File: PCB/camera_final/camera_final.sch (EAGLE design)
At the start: 4 parts

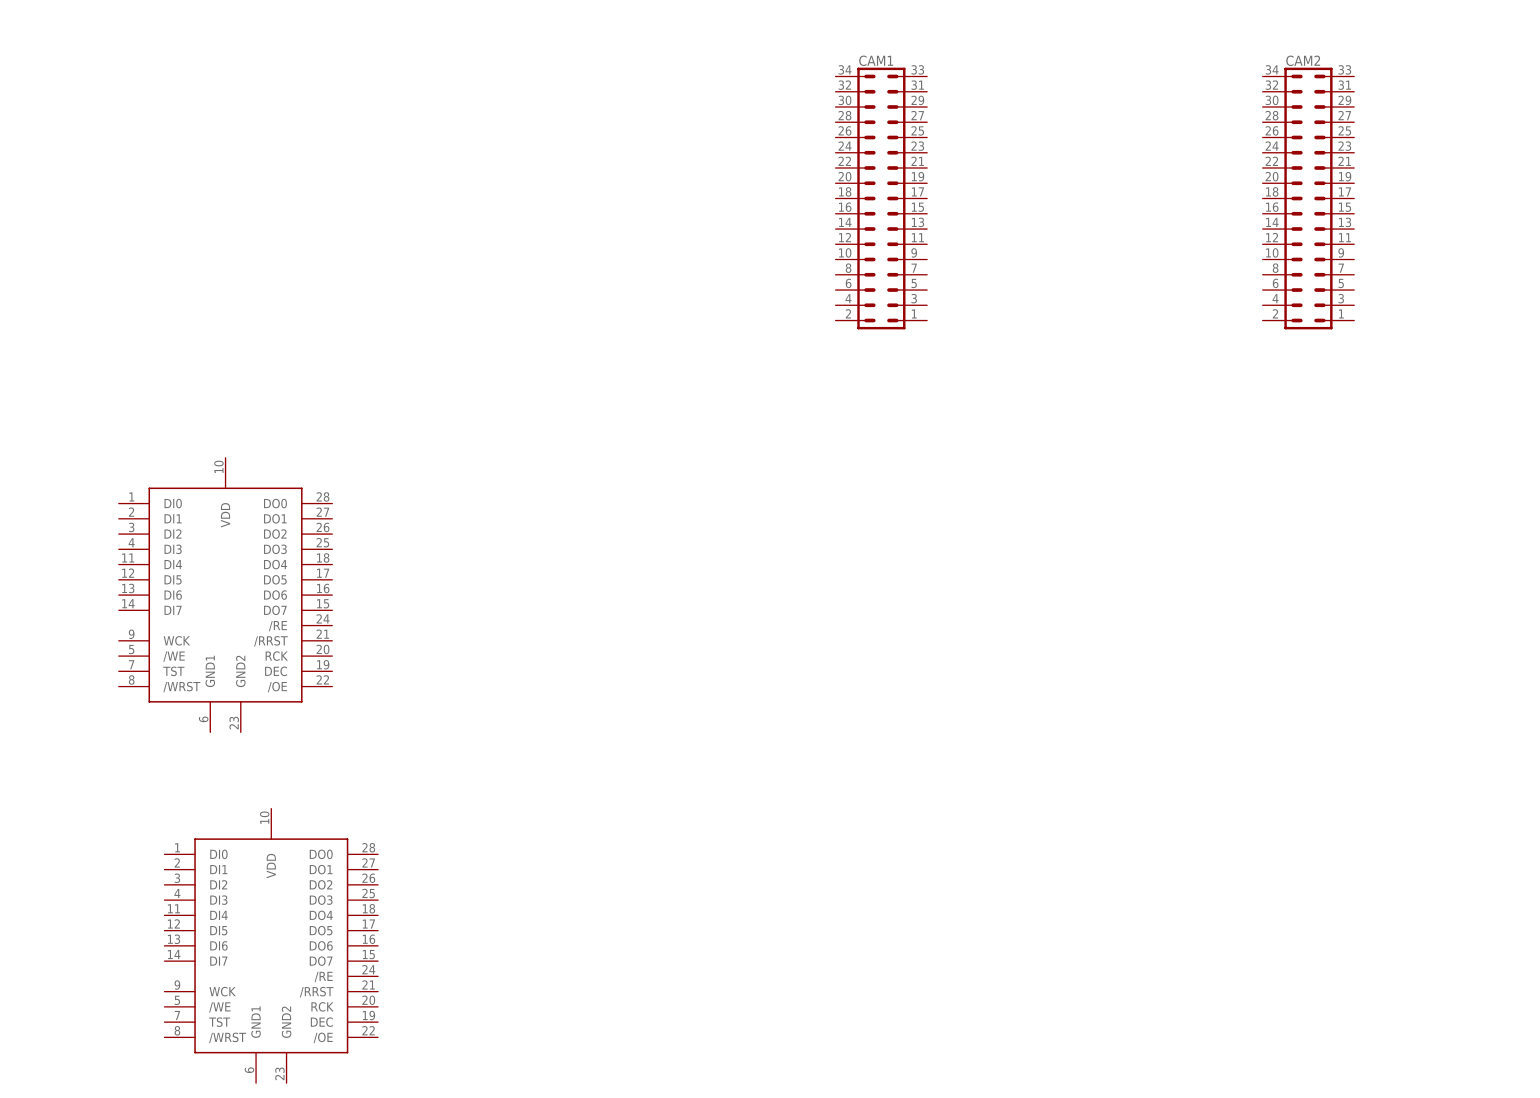
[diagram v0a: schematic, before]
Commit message: final stereo cam schematic, started layout
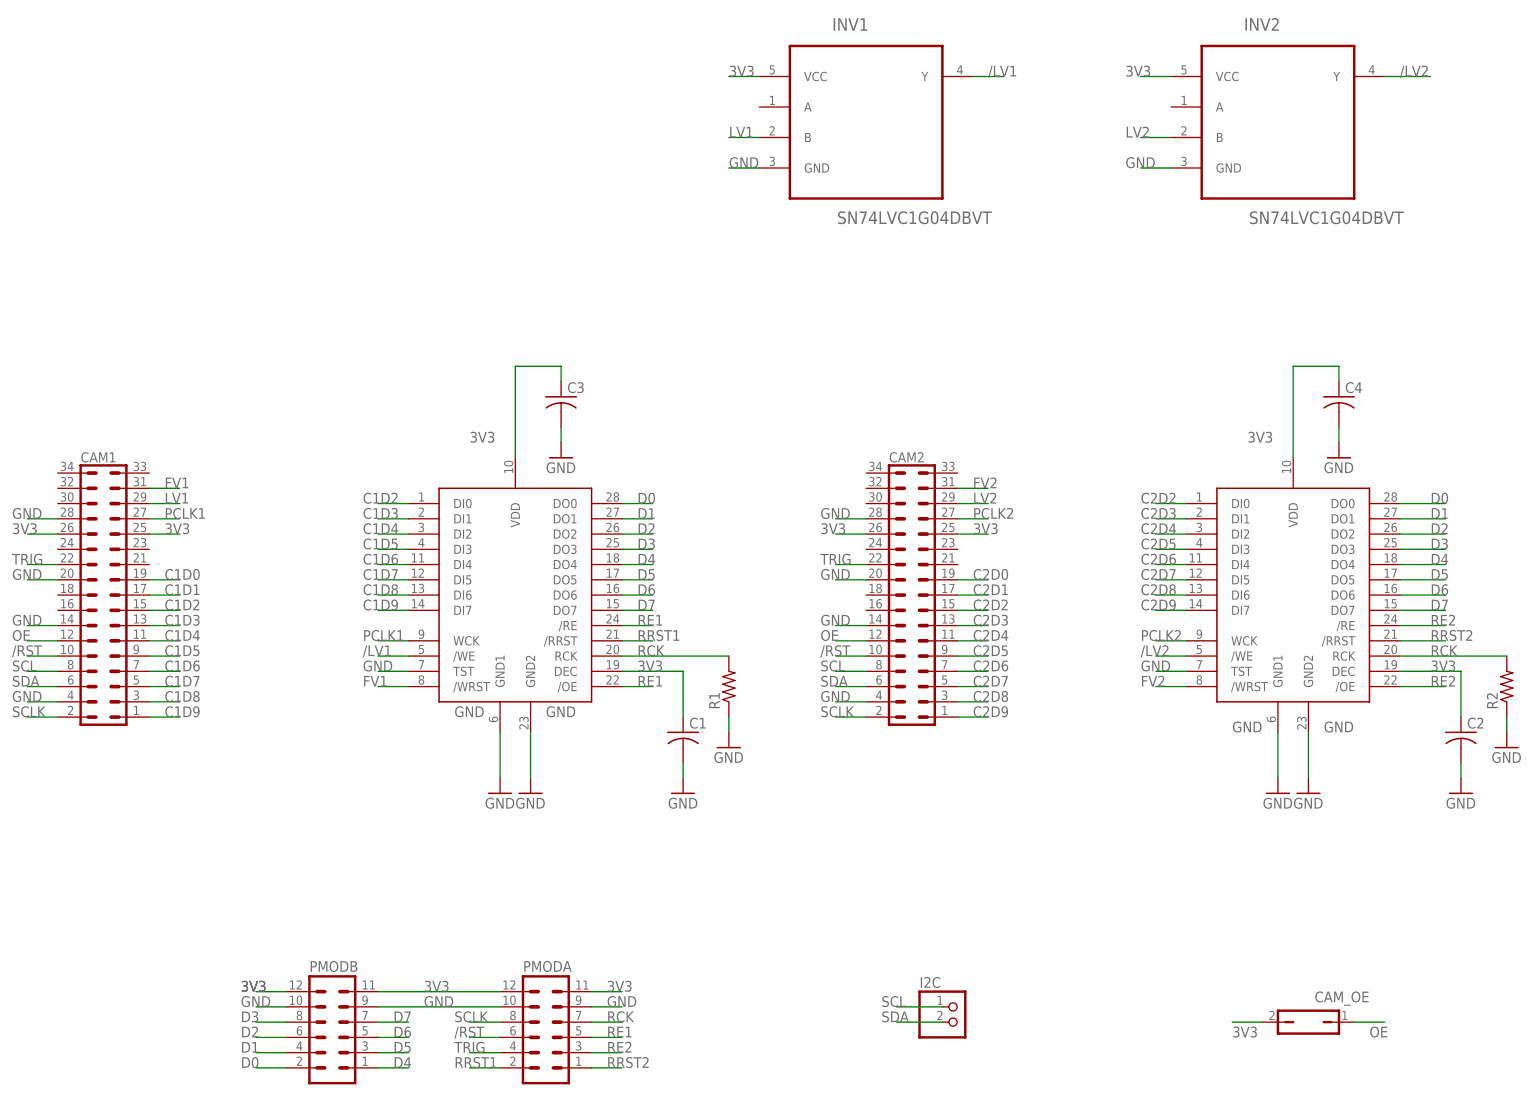
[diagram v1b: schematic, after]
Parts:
- added C1, C2, C3, C4: (no value), adafruit:C-USC0805K
- added CAM_OE: (no value), jumper:JP1Q
- added I2C: (no value), pinhead:PINHD-1X2
- added INV1, INV2: SN74LVC1G04DBVT, Texas Instruments_By_element14_Batch_1:SN74LVC1G08DBVT
- added PMODA, PMODB: (no value), con-lstb:MA06-2
- added R1, R2: (no value), rcl:R-US_R0805
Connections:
- new net /LV1: INV1.Y, U$2./WE
- new net /LV2: INV2.Y, U$1./WE
- new net /RST: CAM1.10, CAM2.10, PMODA.6
- new net 3V3: C1.1, C2.1, C3.1, C4.1, CAM1.25, CAM1.26, CAM2.25, CAM2.26, CAM_OE.2, INV1.VCC, INV2.VCC, PMODA.11, PMODA.12, PMODB.11, PMODB.12, U$1.DEC, U$1.VDD, U$2.DEC, U$2.VDD
- new net C1D0: CAM1.19
- new net C1D1: CAM1.17
- new net C1D2: CAM1.15, U$2.DI0
- new net C1D3: CAM1.13, U$2.DI1
- new net C1D4: CAM1.11, U$2.DI2
- new net C1D5: CAM1.9, U$2.DI3
- new net C1D6: CAM1.7, U$2.DI4
- new net C1D7: CAM1.5, U$2.DI5
- new net C1D8: CAM1.3, U$2.DI6
- new net C1D9: CAM1.1, U$2.DI7
- new net C2D0: CAM2.19
- new net C2D1: CAM2.17
- new net C2D2: CAM2.15, U$1.DI0
- new net C2D3: CAM2.13, U$1.DI1
- new net C2D4: CAM2.11, U$1.DI2
- new net C2D5: CAM2.9, U$1.DI3
- new net C2D6: CAM2.7, U$1.DI4
- new net C2D7: CAM2.5, U$1.DI5
- new net C2D8: CAM2.3, U$1.DI6
- new net C2D9: CAM2.1, U$1.DI7
- new net D0: PMODB.2, U$1.DO0, U$2.DO0
- new net D1: PMODB.4, U$1.DO1, U$2.DO1
- new net D2: PMODB.6, U$1.DO2, U$2.DO2
- new net D3: PMODB.8, U$1.DO3, U$2.DO3
- new net D4: PMODB.1, U$1.DO4, U$2.DO4
- new net D5: PMODB.3, U$1.DO5, U$2.DO5
- new net D6: PMODB.5, U$1.DO6, U$2.DO6
- new net D7: PMODB.7, U$1.DO7, U$2.DO7
- new net FV1: CAM1.31, U$2./WRST
- new net FV2: CAM2.31, U$1./WRST
- new net GND: C1.2, C2.2, C3.2, C4.2, CAM1.14, CAM1.20, CAM1.28, CAM1.4, CAM2.14, CAM2.20, CAM2.28, CAM2.4, INV1.GND, INV2.GND, PMODA.10, PMODA.9, PMODB.10, PMODB.9, R1.1, R2.1, U$1.GND1, U$1.GND2, U$1.TST, U$2.GND1, U$2.GND2, U$2.TST
- new net LV1: CAM1.29, INV1.B
- new net LV2: CAM2.29, INV2.B
- new net OE: CAM1.12, CAM2.12, CAM_OE.1
- new net PCLK1: CAM1.27, U$2.WCK
- new net PCLK2: CAM2.27, U$1.WCK
- new net RCK: PMODA.7, R1.2, R2.2, U$1.RCK, U$2.RCK
- new net RE1: PMODA.5, U$2./OE, U$2./RE
- new net RE2: PMODA.3, U$1./OE, U$1./RE
- new net RRST1: PMODA.2, U$2./RRST
- new net RRST2: PMODA.1, U$1./RRST
- new net SCL: CAM1.8, CAM2.8, I2C.1
- new net SCLK: CAM1.2, CAM2.2, PMODA.8
- new net SDA: CAM1.6, CAM2.6, I2C.2
- new net TRIG: CAM1.22, CAM2.22, PMODA.4
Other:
- moved on the sheet: CAM1, CAM2

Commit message: semi-finalized layout
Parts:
- removed R2: (no value), rcl:R-US_R0805
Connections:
- net GND: no longer R2.1
- net RCK: no longer R2.2
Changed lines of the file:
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@@
 <part name="I2C" library="pinhead" deviceset="PINHD-1X2" device=""/>
 <part name="R1" library="rcl" deviceset="R-US_" device="R0805"/>
-<part name="R2" library="rcl" deviceset="R-US_" device="R0805"/>
 <part name="GND1" library="SparkFun-Aesthetics" deviceset="GND" device=""/>
 <part name="GND2" library="SparkFun-Aesthetics" deviceset="GND" device=""/>
-<part name="GND3" library="SparkFun-Aesthetics" deviceset="GND" device=""/>
 <part name="GND4" library="SparkFun-Aesthetics" deviceset="GND" device=""/>
 <part name="GND5" library="SparkFun-Aesthetics" deviceset="GND" device=""/>
@@
 <instance part="I2C" gate="G$1" x="170.18" y="40.64"/>
 <instance part="R1" gate="G$1" x="132.08" y="96.52" rot="R90"/>
-<instance part="R2" gate="G$1" x="261.62" y="96.52" rot="R90"/>
 <instance part="GND1" gate="1" x="223.52" y="78.74"/>
 <instance part="GND2" gate="1" x="228.6" y="78.74"/>
-<instance part="GND3" gate="1" x="261.62" y="86.36"/>
 <instance part="GND4" gate="1" x="132.08" y="86.36"/>
 <instance part="GND5" gate="1" x="99.06" y="78.74"/>
@@
 </segment>
 <segment>
-<pinref part="R2" gate="G$1" pin="1"/>
-<pinref part="GND3" gate="1" pin="GND"/>
-<wire x1="261.62" y1="91.44" x2="261.62" y2="88.9" width="0.1524" layer="91"/>
-</segment>
-<segment>
 <pinref part="R1" gate="G$1" pin="1"/>
 <pinref part="GND4" gate="1" pin="GND"/>
@@
 <pinref part="U$1" gate="G$1" pin="RCK"/>
 <label x="248.92" y="101.6" size="1.778" layer="95"/>
-<pinref part="R2" gate="G$1" pin="2"/>
 <wire x1="243.84" y1="101.6" x2="261.62" y2="101.6" width="0.1524" layer="91"/>
 </segment>
